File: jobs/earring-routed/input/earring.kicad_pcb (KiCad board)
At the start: 4 copper layers, 30.5 x 35.8 mm, 167 parts, among them J1 USB-C, Q1 ALS-PT19, Q10 BSS138W, Q2 CJ2101, Q3 BSS138W, Q4 LBSS84WT1G, Q5 BSS138W, Q6 BSS138W, Q7 BSS138W, Q8 CJ2101, Q9 BSS138W, SW2 PWR, U1 RP2350A, U10 TPS22913, U2 LGS4056H, U3 NCP730-3.3, U4 TPS22913, U5 USBLC6-2P6, U6 LSM6DS3TR-C, U7 W25Q16JVUXIQ, U8 74LVC2G14, U9 TPS22913, Y1 12MHz

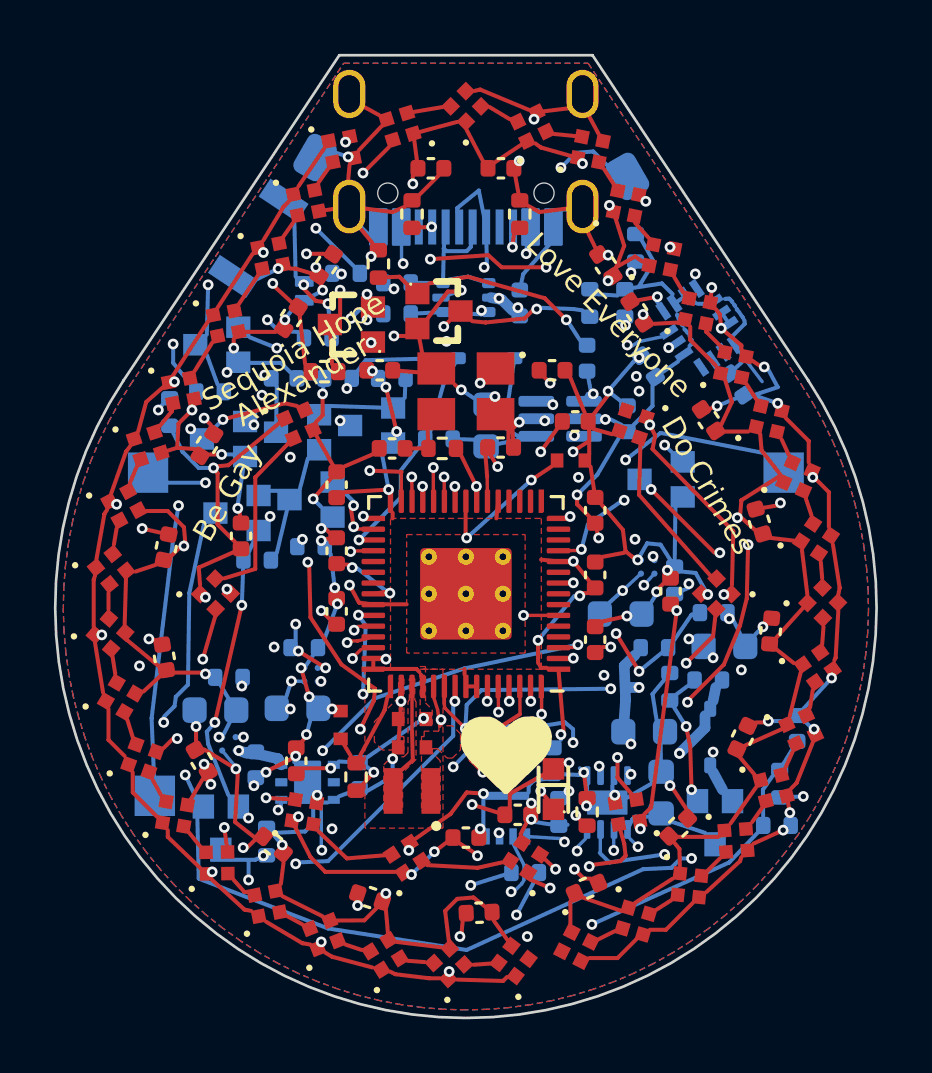
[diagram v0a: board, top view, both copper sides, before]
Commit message: Core: differential pairs routed coupled; both boards re-solved with their USB pairs
--diff-pairs finds pairs by net name (USB_DP/USB_DM, USB_C_DP/USB_C_DN, CLK_P/CLK_N, A+/A-),
takes a pad of each net close together as a pair's end, and routes each run between ends as one
centreline, wide enough for both tracks and the class's diff-pair gap, on a single layer; the
two tracks are laid along it and the router adds the pad legs. Runs go after the fine-pitch
escapes, so they block no pins, and are kept apart from copper the router may rip or pull.
The studio turns it on by default ("Route USB pairs side by side").

The cleanup cuts a track loose at both ends back to its outermost joints and cuts a tail back
to a joint already inside it, so no pair run is left dangling.

Re-solved (KiCad: 0 unconnected, 0 errors): earring-routed with USB_DP/DM 86%/78% coupled,
earring-locked-routed 92%/79%, bluebuzz-routed USB_DP/DM 81%/80% with 0.18 mm skew (the
hand-routed board: 31%). From bare pads, one thread: earring 5 of 6 seeds connected (was 4),
bluebuzz 6 of 6. examples/pair_check measures coupling.

Co-Authored-By: Claude Opus 5.5 (1M context) <noreply@anthropic.com>
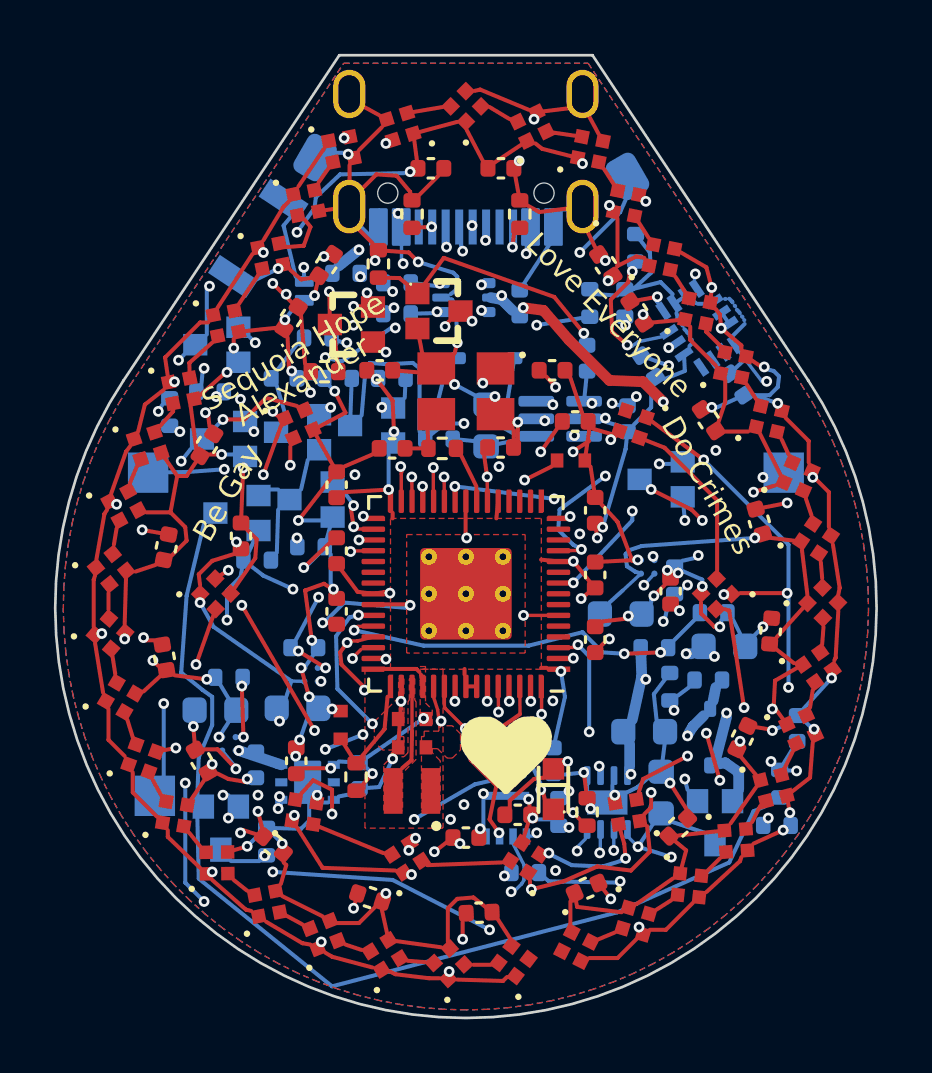
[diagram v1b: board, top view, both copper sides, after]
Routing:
- net LED_EN_L: track 16.5 -> 44.0 mm, vias 4 -> 7
- net VSYS: track 28.1 -> 52.8 mm
- net USB_DM: track 41.4 -> 21.5 mm, vias 7 -> 3
- net USB_DP: track 36.9 -> 18.1 mm, vias 4 -> 2
- net VLED_C: track 62.3 -> 77.3 mm, vias 14 -> 19
- net BOOTSEL: track 22.4 -> 8.48 mm, vias 4 -> 3
- net VBSENSE: track 41.9 -> 32.5 mm, vias 3 -> 4
- net BTN_SENSE: track 12.2 -> 21.2 mm
- net GND: track 204.5 -> 212.5 mm, vias 84 -> 86
- net LEDC_D2: track 11.8 -> 19.2 mm
- net QSPI_SD1: track 9.45 -> 16.7 mm, vias 2 -> 4
- net SWDIO: track 33.1 -> 26.5 mm, vias 3 -> 4
- net VBATT: track 52.7 -> 58.9 mm, vias 8 -> 9
- net CHRG: track 32.9 -> 26.7 mm, vias 6 -> 5
- net PWR_EN: track 34.4 -> 30.1 mm, vias 5 -> 8
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
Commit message: Core: differential pairs length-matched, and the short pair coupled; jobs re-solved
Length matching (grid::match_lengths): after the cleanup each pair's nets are measured end to
end along their copper and the shorter one is given bumps, one at a time, the tallest that lays,
on uncoupled tracks first; a bump that does not reduce the skew is undone.

The short pair: pins of a pair whose ends share a layer are left out of the fan-out, a run's
layer is chosen by cost (length, a price per via its ends need, how far from the pins it
starts) with each layer trying its nearest start ring first, and pair runs may cross pours,
kept block planes included, to be refilled round them. bluebuzz's resistor-to-RP2350 pair now
runs side by side on F.Cu with no via.

Re-solved (KiCad: 0 unconnected, 0 errors, no part moved): earring-routed, pairs 0.00 and 0.16
mm apart; earring-locked-routed 0.00 and 0.00; bluebuzz-routed 0.00 (76%/72% side by side)
and 0.13 mm (58%/60%). job.json `args` gives the studio the seed each job routes best with.

Co-Authored-By: Claude Opus 5.5 (1M context) <noreply@anthropic.com>
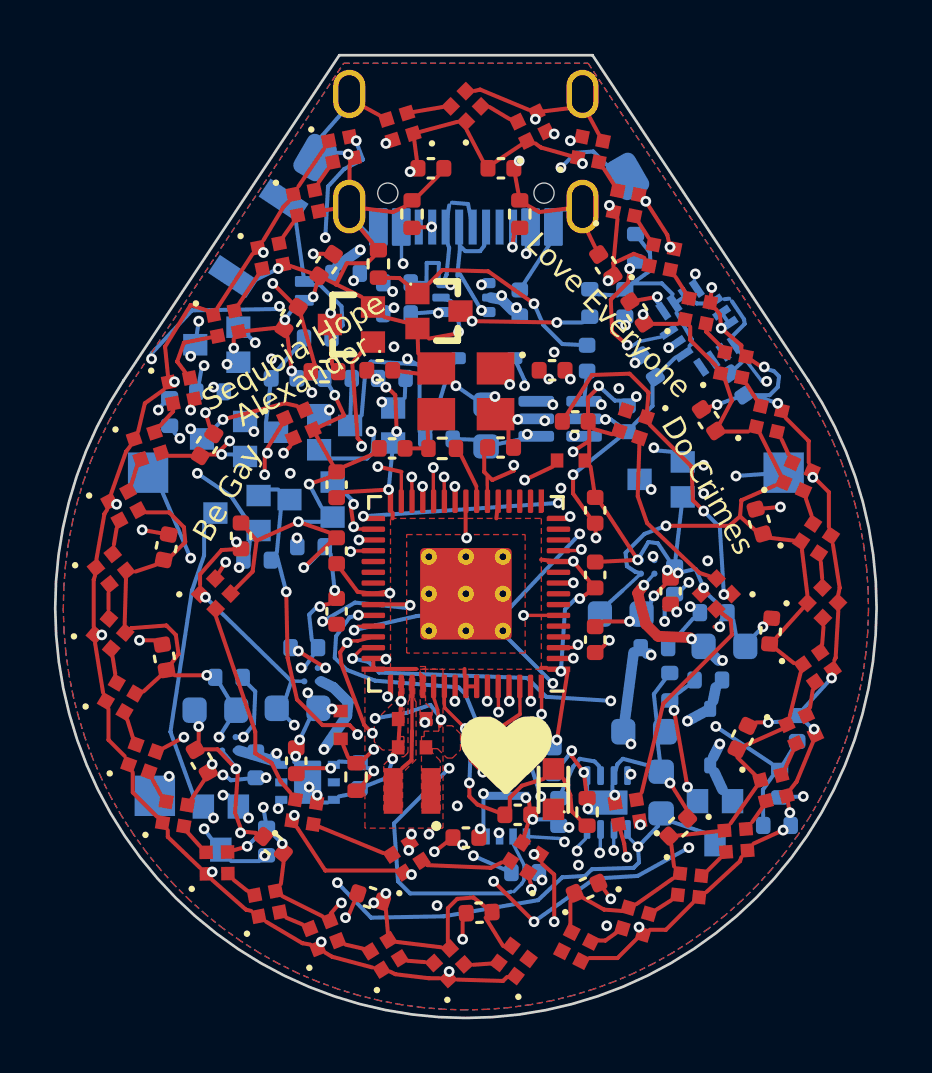
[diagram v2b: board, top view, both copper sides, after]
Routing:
- net LATCH_G: track 3.03 -> 71.3 mm, vias 0 -> 13
- net LED_EN_L: track 44.0 -> 16.2 mm, vias 7 -> 2
- net VLED_C: track 77.3 -> 61.4 mm, vias 19 -> 15
- net VSYS: track 52.8 -> 39.6 mm
- net VBSENSE: track 32.5 -> 20.6 mm, vias 4 -> 3
- net LEDC_D2: track 19.2 -> 7.30 mm, vias 2 -> 0
- net LEDC_D5: track 4.27 -> 14.8 mm, vias 2 -> 3
- net BOOTSEL_SW: track 21.4 -> 31.6 mm, vias 5 -> 4
- net SWDIO: track 26.5 -> 18.4 mm, vias 4 -> 2
- net USB_DP: track 18.1 -> 24.8 mm
- net VDD_CORE: track 21.2 -> 27.6 mm, vias 7 -> 8
- net RUN: track 22.9 -> 28.5 mm
- net GND: track 212.5 -> 217.8 mm, vias 86 -> 87
- net CHRG: track 26.7 -> 21.9 mm, vias 5 -> 3
- net VLED_R: track 66.6 -> 62.4 mm, vias 11 -> 7
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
